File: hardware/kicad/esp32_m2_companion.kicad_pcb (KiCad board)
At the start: 6 copper layers, 22 x 42 mm, 53 parts, among them J1 M2_KEYB_2242_EDGE, J3 Conn_01x04, J4 Conn_01x08, Q1 SSM6N56FE, Q2 SSM6N56FE, Q3 SSM6N56FE, U1 USBLC6-2SC6, U2 ESP32-S3-WROOM-1, U3 TMUX1511_RSV, U4 TMUX1511_RSV, U5 TMUX1511_RSV, U6 TPS259470A_RPW

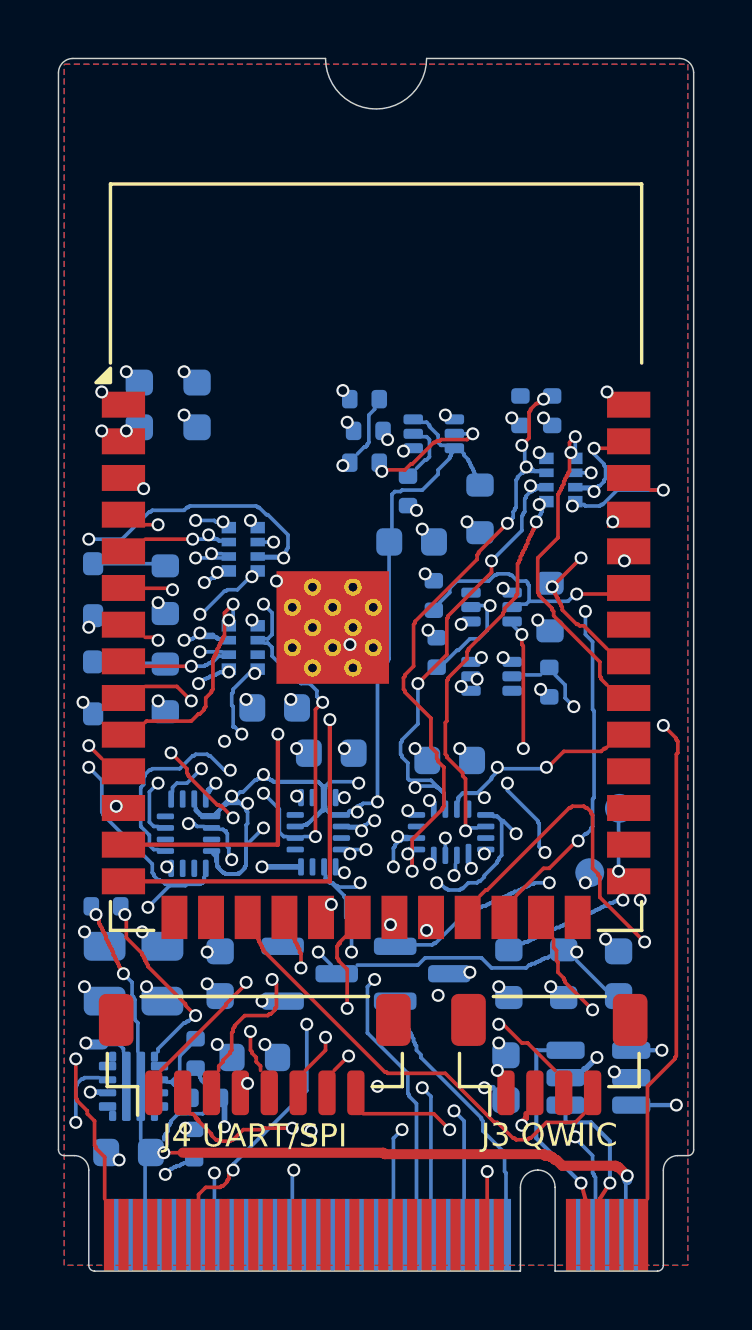
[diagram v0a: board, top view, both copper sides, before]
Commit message: v2 GATE V3 (wip): USB off the switch strip, eFuse cluster re-placed, finger fan-in
- Vias: 0.2 mm drill everywhere new (free with 0.45 pad); 0.35/0.2 vias only
  for switch/array escapes + EXP finger fan-in (owner-approved JLC
  "0.2mm/(0.3/0.35mm)" option, ~+$0.5/board @100). Hole-to-copper 0.2 mm
  (JLC capabilities "Inner layer via hole to copper clearance 0.2mm").
- USB_D_P/N: In2 down the module's left pad column, via-in-pad on U2.13/14
  (the F.Cu leg ran under U4/U5 and blocked every escape via).
- Router: nets may change layer through their own vias (escape vias were
  unusable); gold-finger keep-out (no copper between fingers); --via,
  --drill, --escape-only, --first, --thin.
- eFuse cluster: C1/C2 bulk caps moved near the module 3V3 pin, U6 up 1.7 mm,
  C14/R34 out of the J1 courtyard; +3V3_M2 trunk hand-routed + locked
  (v2_power_route.py); EXP_7/9/10 finger fan-in hand-routed (v2_fanin_route.py).
- RPW footprint: L-pin leg overlaps its bar (pin 1 EN was split for KiCad).
- v2_prune_branches.py: dead-branch pruning by copper overlap (pruning on
  KiCad's dangling flag unravelled complete nets).
Open: +3V3_EFUSE, +3V3_M2 thin link, CONFIG_2, IO10, EXP_9_S, LED_1_n, silk.

Co-Authored-By: Claude Opus 5.5 <noreply@anthropic.com>
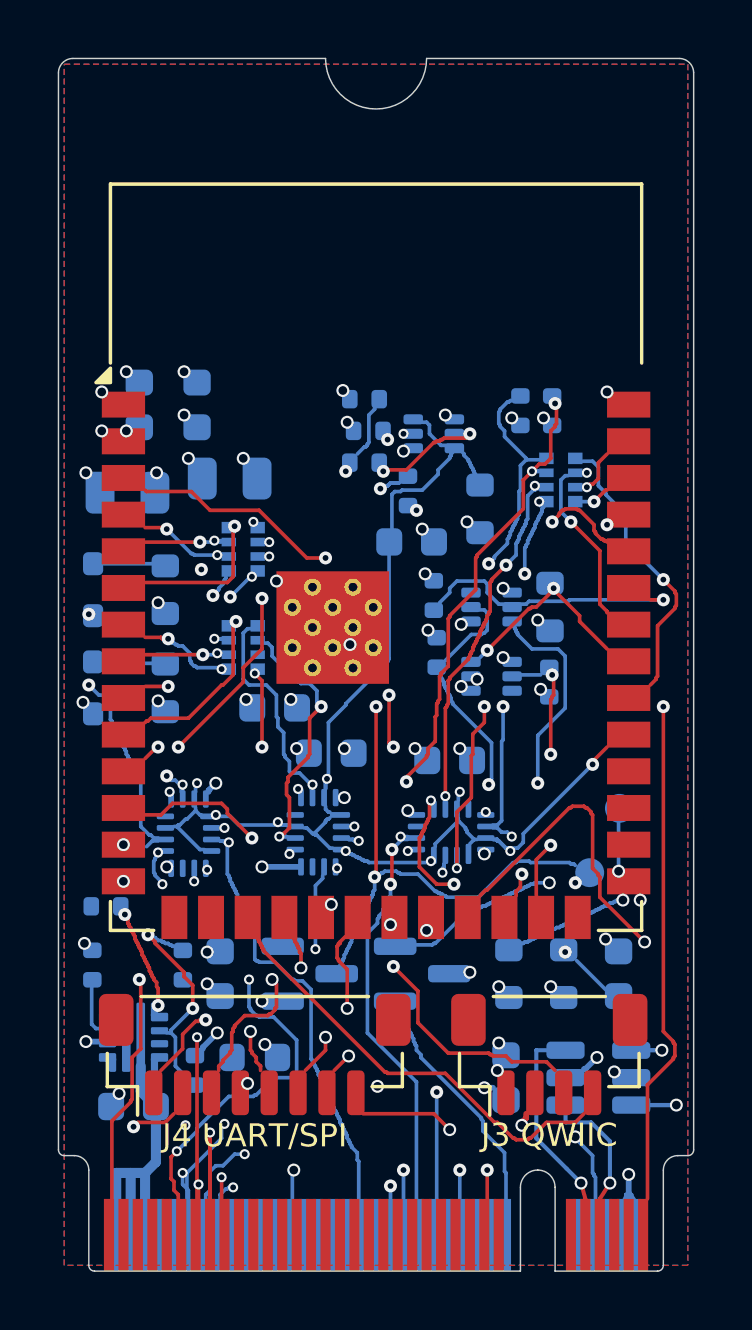
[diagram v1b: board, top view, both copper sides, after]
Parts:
- moved C2 17.3 mm to (94.9, 122.5), turned to 0 degrees
- moved C1 16.7 mm to (91.4, 123.0), turned to 0 degrees
- moved R34 7.13 mm to (90.2, 139.4)
- moved R31 3.09 mm to (93.3, 139.4)
- moved U6 1.70 mm to (91.6, 141.9)
- moved C14 1.60 mm to (91.6, 144.3)
- moved R32 1.02 mm to (93.7, 143.0), turned to 90 degrees
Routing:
- net EXP_OE: track 55.7 -> 36.2 mm, vias 15 -> 9
- net EXP_6: track 33.2 -> 13.9 mm, vias 2 -> 3
- net EXP_11: track 0.05 -> 18.8 mm, vias 1 -> 3
- net EXP_0_S: track 0.42 -> 19.1 mm, vias 2 -> 3
- net +3V3_M2: track 28.4 -> 9.92 mm, vias 4 -> 1
- net EXP_6_S: track 0.30 -> 18.0 mm, vias 1 -> 2
- net EXP_8: track 0.00 -> 15.7 mm, vias 0 -> 2
- net EXP_7: track 1.42 -> 17.1 mm, vias 1 -> 2
- net EXP_2: track 0.05 -> 15.5 mm, vias 1 -> 3
- net EXP_4: track 0.00 -> 15.3 mm, vias 0 -> 1
- net EXP_10: track 0.00 -> 14.6 mm, vias 0 -> 3
- net RXD0: track 28.7 -> 41.7 mm
- net EXP_7_S: track 0.05 -> 12.2 mm, vias 1 -> 3
- net EXP_5: track 0.00 -> 12.1 mm, vias 0 -> 3
- net EXP_5_S: track 27.4 -> 16.2 mm, vias 4 -> 3
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
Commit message: v2 GATE V3 (wip): routing complete - 0 unconnected, copper DRC clean
- All nets routed; make drc: 0 unconnected, no copper violations (92 left,
  all silkscreen - next step). make check PASS.
- eFuse: FB1 moved right above U6 (OUT -> FB1.1 hop, locked); R34 to FB1's
  old spot; IN sense branches leave from the trunk side.
- USBH3_D_N finger-9 via moved off finger 10 (v2_usbh3_dn_reroute.py,
  0.35/0.2 via, +0.2 mm) so LED_1_n (finger 10) can escape; GND finger 11
  keeps its F pour path (rule areas GND11_STRIP / GND11_BAND).
- GND fingers 3/5, 11, 57 were floating on the card side: fingers 2/4
  +3V3_M2 via moved up 1.9 mm, +3V3_M2 2/4 link re-routed off the finger
  tops, finger 57 stub + via, island stitching (v2_stitch_islands.py).
- Router: terminals include copper already attached to the pad (escape
  stubs / hand fan-ins); rule areas only block their own layers; --debug /
  --dump reachability; ripnets --keep-locked; zoom draws zone fills.
- v2_tie_vias.py: tie / drop KiCad 'dangling' vias (single-layer escapes).
- DRU: gnd_single_spoke_pads (R28.2, C11.2, Q1.4 via-backed; J1.21 no room).

Co-Authored-By: Claude Opus 5.5 <noreply@anthropic.com>
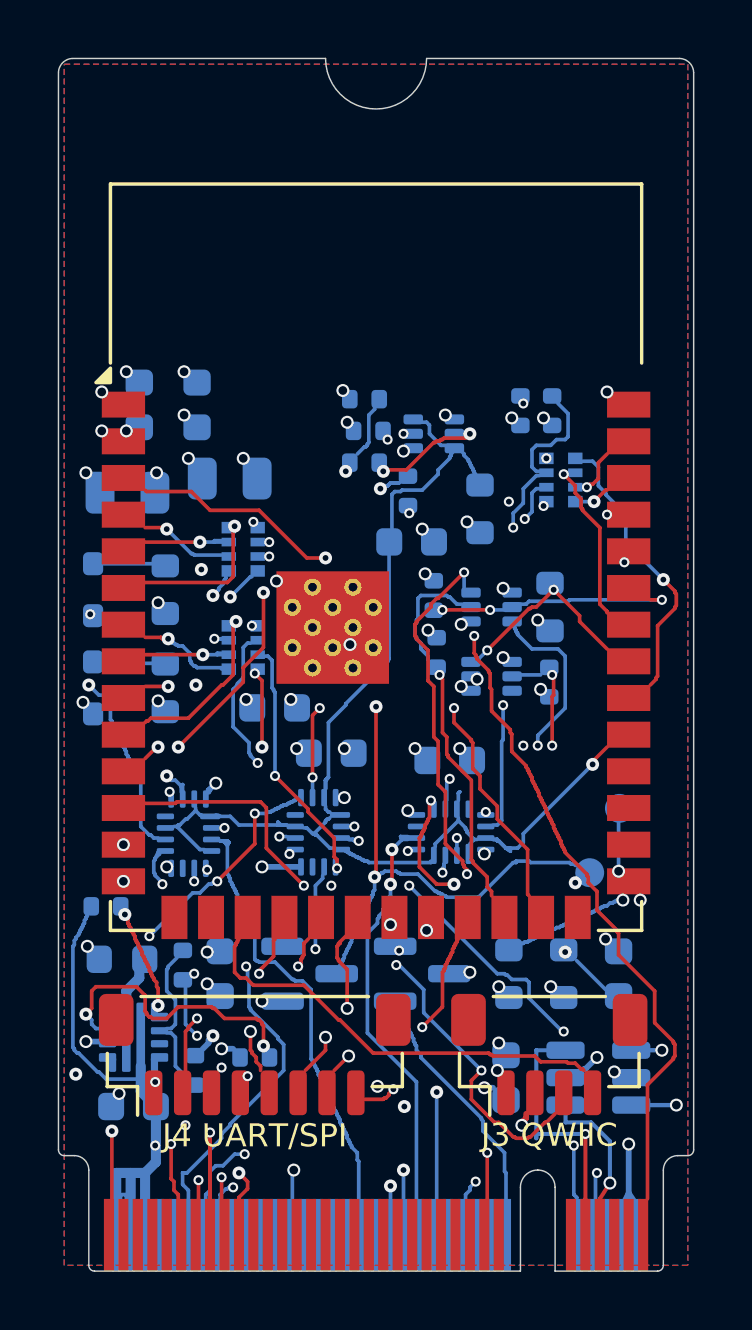
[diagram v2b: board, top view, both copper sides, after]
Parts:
- moved R34 6.47 mm to (95.8, 142.6), turned to 180 degrees
- moved FB1 5.72 mm to (91.2, 139.2), turned to 180 degrees
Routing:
- net +3V3_M2: track 9.92 -> 50.1 mm, vias 1 -> 6
- net LED_1_n: track 0.00 -> 25.8 mm, vias 0 -> 3
- net IO21: track 24.2 -> 7.36 mm
- net RXD0: track 41.7 -> 25.4 mm, vias 2 -> 4
- net TXD0: track 26.8 -> 38.0 mm, vias 2 -> 3
- net EXP_9_S: track 0.00 -> 8.44 mm, vias 1 -> 2
- net EFUSE_ILM: track 1.61 -> 9.73 mm, vias 0 -> 2
- net EXP_9: track 18.7 -> 13.0 mm, vias 3 -> 2
- net W_DISABLE1_n: track 17.1 -> 12.0 mm
- net LED_STATUS_n: track 28.6 -> 25.5 mm, vias 4 -> 2
- net IO8: track 19.1 -> 21.8 mm, vias 2 -> 3
- net EFUSE_OVLO: track 7.35 -> 4.86 mm, vias 2 -> 0
- net IO11: track 7.40 -> 5.74 mm
- net EXP_0_S: track 19.1 -> 17.5 mm
- net EXP_OE: track 36.2 -> 37.8 mm, vias 9 -> 1
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
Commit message: v2 GATE V3 (wip): silkscreen cleanup - make drc clean (0 violations)
- Revision text v2.0 Rev A 2026-10; rev-B TX/RX/3V3/GND test-point labels
  deleted (TP3-TP6 removed in v2); EN / BOOT moved next to TP1 / TP2.
- All reference labels 0.8 mm / 0.15 (min_text_height), each re-placed at
  the nearest spot clear of pads, other silk and the board edge
  (tools/v2_silk.py); 17 with no legal spot within 2.5 mm hidden (assembly
  drawing keeps them): C1, D4, FB1, Q2, Q3, R23, R25, R27, R28, R3, R31,
  R4, RN2, RN3, TP1, TP2 (EN/BOOT labels), U6.
- make drc: 0 violations, 0 unconnected, 1 excluded (U2 serialization).

Co-Authored-By: Claude Opus 5.5 <noreply@anthropic.com>
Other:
- board text added: "v2.0 Rev A 2026-10"
- board text removed: "3V3"
- board text removed: "GND"
- board text removed: "RX"
- board text removed: "TX"
- board text removed: "v1.0 Rev B 2026-10"

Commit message: v2 GATE V3 (wip): owner silkscreen edits - logo top-right, name/version left-aligned, 'Designed in Italy'
make drc: 2 text_height warnings ('Designed in Italy' 0.5 mm, version 0.6 mm
< 0.8 mm min_text_height) - resolved in the next commit.

Co-Authored-By: Claude Opus 5.5 <noreply@anthropic.com>
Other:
- board text added: "Designed in Italy"
- board text removed: "Stefano Viola"

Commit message: v2 GATE V3 (wip): branding - name on top, version/origin/website on the back
- Top: board name split around the mounting notch ("ESP32-M2" | "COMPANION",
  0.9 mm) in the only free top strip (edge to module silk, y 108.0-112.3).
- Back: owner's logo + version / "Designed in Italy" / samnium.tech, 0.8 mm
  (DRC min_text_height; the owner's 0.5/0.6 mm drafts were below it).
- tools/v2_brand.py (idempotent). make drc: 0 violations, 0 unconnected.

Co-Authored-By: Claude Opus 5.5 <noreply@anthropic.com>
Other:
- board text added: "COMPANION"
- board text added: "ESP32-M2"
- board text added: "samnium.tech"
- board text removed: "ESP32-M2-COMPANION"
